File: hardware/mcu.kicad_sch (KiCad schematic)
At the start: 0 parts

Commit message: Kicad şema düzenlemesi yapıldı.
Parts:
- added U4: STM32F103RCTx, Package_QFP:LQFP-64_10x10mm_P0.5mm, symbol MCU_ST_STM32F1:STM32F103RCTx
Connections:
- new net: U4.18 (VSS), U4.31 (VSS), U4.47 (VSS), U4.63 (VSS)
- new net BTN_ACTIVATE: U4.39 (PC8)
- new net BTN_DEACTIVATE: U4.40 (PC9)
- new net BTN_IO: U4.38 (PC7)
- new net I2C_SCL: U4.58 (PB6)
- new net I2C_SDA: U4.59 (PB7)
- new net MCU_ADC_IN: U4.14 (PA0)
- new net MCU_ERROR_LED: U4.36 (PB15)
- new net MCU_RELAY: U4.34 (PB13)
- new net MCU_STATUS_LED: U4.35 (PB14)
- new net RCC_OSC32_IN: U4.3 (PC14)
- new net RCC_OSC32_OUT: U4.4 (PC15)
- new net RCC_OSC_IN: U4.5 (PD0)
- new net RCC_OSC_OUT: U4.6 (PD1)
- new net SPI1_MISO: U4.22 (PA6)
- new net SPI1_MOSI: U4.23 (PA7)
- new net SPI1_SCK: U4.21 (PA5)
- new net SYS_JTCK_SWCLK: U4.49 (PA14)
- new net SYS_JTMS_SWDIO: U4.46 (PA13)
- new net UART_RX: U4.52 (PC11)
- new net UART_TX: U4.51 (PC10)
- new net USAR1_RX: U4.43 (PA10)
- new net USART1_TX: U4.42 (PA9)
- new net USART2_RX: U4.17 (PA3)
- new net USART2_TX: U4.16 (PA2)
- new net USART3_RX: U4.30 (PB11)
- new net USART3_TX: U4.29 (PB10)
- new net USB_DM: U4.44 (PA11)
- new net USB_DP: U4.45 (PA12)
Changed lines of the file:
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@@
 (kicad_sch (version 20230121) (generator eeschema)
   (paper "A4")
+  (hierarchical_label "USB_DP" (shape input) (at 160.02 74.93 0) (fields_autoplaced)
+    (effects (font (size 1.27 1.27)) (justify left))
+  )
+  (hierarchical_label "SPI1_MOSI" (shape output) (at 160.02 62.23 0) (fields_autoplaced)
+    (effects (font (size 1.27 1.27)) (justify left))
+  )
+  (hierarchical_label "RCC_OSC32_IN" (shape input) (at 124.46 100.33 180) (fields_autoplaced)
+    (effects (font (size 1.27 1.27)) (justify right))
+  )
+  (hierarchical_label "BTN_DEACTIVATE" (shape output) (at 124.46 87.63 180) (fields_autoplaced)
+    (effects (font (size 1.27 1.27)) (justify right))
+  )
+  (hierarchical_label "USART3_RX" (shape input) (at 160.02 115.57 0) (fields_autoplaced)
+    (effects (font (size 1.27 1.27)) (justify left))
+  )
+  (hierarchical_label "I2C_SDA" (shape bidirectional) (at 160.02 105.41 0) (fields_autoplaced)
+    (effects (font (size 1.27 1.27)) (justify left))
+  )
+  (hierarchical_label "RCC_OSC_OUT" (shape output) (at 124.46 57.15 180) (fields_autoplaced)
+    (effects (font (size 1.27 1.27)) (justify right))
+  )
+  (hierarchical_label "MCU_ADC_IN" (shape input) (at 160.02 44.45 0) (fields_autoplaced)
+    (effects (font (size 1.27 1.27)) (justify left))
+  )
+  (hierarchical_label "MCU_STATUS_LED" (shape output) (at 160.02 123.19 0) (fields_autoplaced)
+    (effects (font (size 1.27 1.27)) (justify left))
+  )
+  (hierarchical_label "RCC_OSC32_OUT" (shape output) (at 124.46 102.87 180) (fields_autoplaced)
+    (effects (font (size 1.27 1.27)) (justify right))
+  )
+  (hierarchical_label "USAR1_RX" (shape input) (at 160.02 69.85 0) (fields_autoplaced)
+    (effects (font (size 1.27 1.27)) (justify left))
+  )
+  (hierarchical_label "MCU_RELAY" (shape output) (at 160.02 120.65 0) (fields_autoplaced)
+    (effects (font (size 1.27 1.27)) (justify left))
+  )
+  (hierarchical_label "USART2_TX" (shape output) (at 160.02 49.53 0) (fields_autoplaced)
+    (effects (font (size 1.27 1.27)) (justify left))
+  )
+  (hierarchical_label "BTN_ACTIVATE" (shape output) (at 124.46 85.09 180) (fields_autoplaced)
+    (effects (font (size 1.27 1.27)) (justify right))
+  )
+  (hierarchical_label "USART2_RX" (shape input) (at 160.02 52.07 0) (fields_autoplaced)
+    (effects (font (size 1.27 1.27)) (justify left))
+  )
+  (hierarchical_label "I2C_SCL" (shape output) (at 160.02 102.87 0) (fields_autoplaced)
+    (effects (font (size 1.27 1.27)) (justify left))
+  )
+  (hierarchical_label "RCC_OSC_IN" (shape input) (at 124.46 54.61 180) (fields_autoplaced)
+    (effects (font (size 1.27 1.27)) (justify right))
+  )
+  (hierarchical_label "USART1_TX" (shape output) (at 160.02 67.31 0) (fields_autoplaced)
+    (effects (font (size 1.27 1.27)) (justify left))
+  )
+  (hierarchical_label "MCU_ERROR_LED" (shape output) (at 160.02 125.73 0) (fields_autoplaced)
+    (effects (font (size 1.27 1.27)) (justify left))
+  )
+  (hierarchical_label "SYS_JTMS_SWDIO" (shape bidirectional) (at 160.02 77.47 0) (fields_autoplaced)
+    (effects (font (size 1.27 1.27)) (justify left))
+  )
+  (hierarchical_label "USB_DM" (shape output) (at 160.02 72.39 0) (fields_autoplaced)
+    (effects (font (size 1.27 1.27)) (justify left))
+  )
+  (hierarchical_label "BTN_IO" (shape output) (at 124.46 82.55 180) (fields_autoplaced)
+    (effects (font (size 1.27 1.27)) (justify right))
+  )
+  (hierarchical_label "USART3_TX" (shape output) (at 160.02 113.03 0) (fields_autoplaced)
+    (effects (font (size 1.27 1.27)) (justify left))
+  )
+  (hierarchical_label "SPI1_SCK" (shape output) (at 160.02 57.15 0) (fields_autoplaced)
+    (effects (font (size 1.27 1.27)) (justify left))
+  )
+  (hierarchical_label "SPI1_MISO" (shape input) (at 160.02 59.69 0) (fields_autoplaced)
+    (effects (font (size 1.27 1.27)) (justify left))
+  )
+  (hierarchical_label "SYS_JTCK_SWCLK" (shape bidirectional) (at 160.02 80.01 0) (fields_autoplaced)
+    (effects (font (size 1.27 1.27)) (justify left))
+  )
+  (hierarchical_label "UART_TX" (shape output) (at 124.46 90.17 180) (fields_autoplaced)
+    (effects (font (size 1.27 1.27)) (justify right))
+  )
+  (hierarchical_label "UART_RX" (shape input) (at 124.46 92.71 180) (fields_autoplaced)
+    (effects (font (size 1.27 1.27)) (justify right))
+  )
+  (symbol (lib_id "MCU_ST_STM32F1:STM32F103RCTx") (at 142.24 87.63 0) (unit 1)
+    (in_bom yes) (on_board yes) (dnp no) (fields_autoplaced)
+    (property "Reference" "U4" (at 146.9741 133.35 0)
+      (effects (font (size 1.27 1.27)) (justify left))
+    )
+    (property "Value" "STM32F103RCTx" (at 146.9741 135.89 0)
+      (effects (font (size 1.27 1.27)) (justify left))
+    )
+    (property "Footprint" "Package_QFP:LQFP-64_10x10mm_P0.5mm" (at 127 130.81 0)
+      (effects (font (size 1.27 1.27)) (justify right) hide)
+    )
+    (property "Datasheet" "https://www.st.com/resource/en/datasheet/stm32f103rc.pdf" (at 142.24 87.63 0)
+      (effects (font (size 1.27 1.27)) hide)
+    )
+    (pin "1")
+    (pin "10")
+    (pin "11")
+    (pin "12")
+    (pin "13")
+    (pin "14")
+    (pin "15")
+    (pin "16")
+    (pin "17")
+    (pin "18")
+    (pin "19")
+    (pin "2")
+    (pin "20")
+    (pin "21")
+    (pin "22")
+    (pin "23")
+    (pin "24")
+    (pin "25")
+    (pin "26")
+    (pin "27")
+    (pin "28")
+    (pin "29")
+    (pin "3")
+    (pin "30")
+    (pin "31")
+    (pin "32")
+    (pin "33")
+    (pin "34")
+    (pin "35")
+    (pin "36")
+    (pin "37")
+    (pin "38")
+    (pin "39")
+    (pin "4")
+    (pin "40")
+    (pin "41")
+    (pin "42")
+    (pin "43")
+    (pin "44")
+    (pin "45")
+    (pin "46")
+    (pin "47")
+    (pin "48")
+    (pin "49")
+    (pin "5")
+    (pin "50")
+    (pin "51")
+    (pin "52")
+    (pin "53")
+    (pin "54")
+    (pin "55")
+    (pin "56")
+    (pin "57")
+    (pin "58")
+    (pin "59")
+    (pin "6")
+    (pin "60")
+    (pin "61")
+    (pin "62")
+    (pin "63")
+    (pin "64")
+    (pin "7")
+    (pin "8")
+    (pin "9")
+    (instances
+      (project "drip-irrigation-sys-cc"
+        (path "/41708c1e-19b2-4374-83f2-108076d82b45/c9797de2-f042-4c0a-b92d-0b1dd104a99b"
+          (reference "U4") (unit 1)
+        )
+      )
+    )
+  )
 )

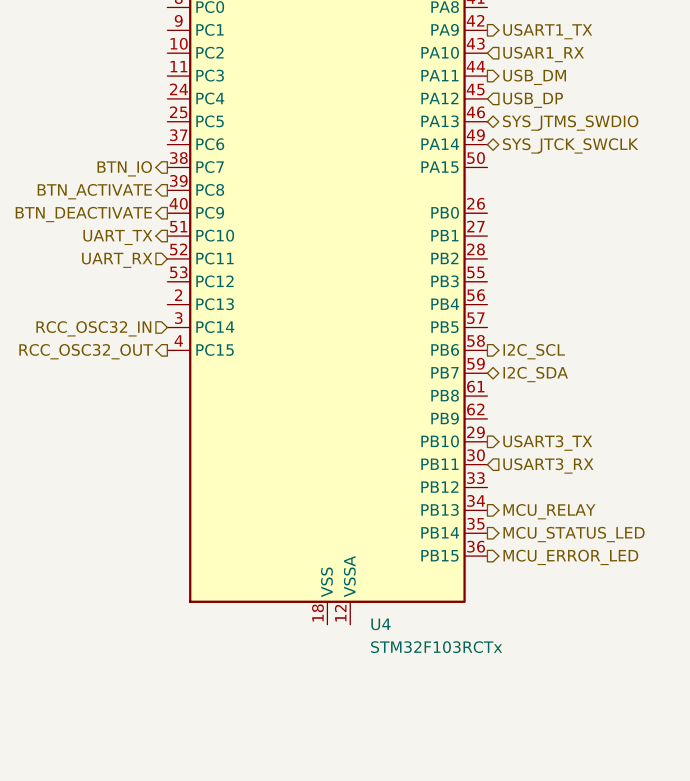
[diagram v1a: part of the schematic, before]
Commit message: Kicad Power Modülü Tamamlandı.
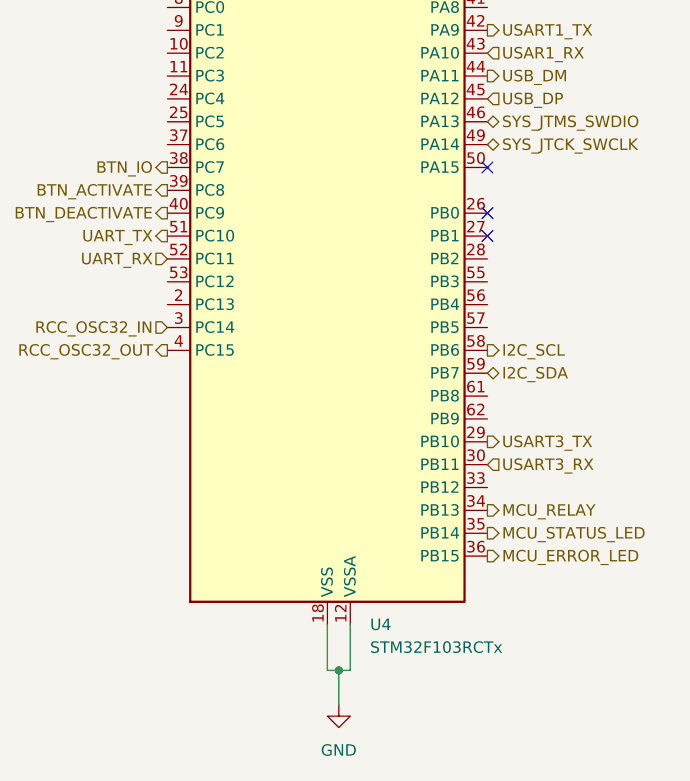
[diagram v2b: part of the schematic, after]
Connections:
- net GND: now reaches U4.12 (VSSA)
- net GND: now also U4.18 (VSS), U4.31 (VSS), U4.47 (VSS), U4.63 (VSS)
- no-connect marks 0 -> 3
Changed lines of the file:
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@@
 (kicad_sch (version 20230121) (generator eeschema)
   (paper "A4")
+  (junction (at 143.51 138.43) (diameter 0) (color 0 0 0 0)
+  )
+  (no_connect (at 160.02 87.63))
+  (no_connect (at 160.02 82.55))
+  (no_connect (at 160.02 90.17))
+  (wire (pts (xy 143.51 138.43) (xy 144.78 138.43))
+    (stroke (width 0) (type default))
+  )
+  (wire (pts (xy 144.78 133.35) (xy 144.78 138.43))
+    (stroke (width 0) (type default))
+  )
+  (wire (pts (xy 142.24 133.35) (xy 142.24 138.43))
+    (stroke (width 0) (type default))
+  )
+  (wire (pts (xy 143.51 138.43) (xy 143.51 142.24))
+    (stroke (width 0) (type default))
+  )
+  (wire (pts (xy 142.24 138.43) (xy 143.51 138.43))
+    (stroke (width 0) (type default))
+  )
   (hierarchical_label "USB_DP" (shape input) (at 160.02 74.93 0) (fields_autoplaced)
     (effects (font (size 1.27 1.27)) (justify left))
@@
         )
       )
+    )
+  )
+  (symbol (lib_id "power:GND") (at 143.51 142.24 0) (unit 1)
+    (in_bom yes) (on_board yes) (dnp no) (fields_autoplaced)
+    (property "Reference" "#PWR06" (at 143.51 148.59 0)
+      (effects (font (size 1.27 1.27)) hide)
+    )
+    (property "Value" "GND" (at 143.51 147.32 0)
+      (effects (font (size 1.27 1.27)))
+    )
+    (property "Footprint" "" (at 143.51 142.24 0)
+      (effects (font (size 1.27 1.27)) hide)
+    )
+    (property "Datasheet" "" (at 143.51 142.24 0)
+      (effects (font (size 1.27 1.27)) hide)
+    )
+    (pin "1")
+    (instances
+      (project "drip-irrigation-sys-cc"
+        (path "/41708c1e-19b2-4374-83f2-108076d82b45/c9797de2-f042-4c0a-b92d-0b1dd104a99b"
+          (reference "#PWR06") (unit 1)
+        )
+      )

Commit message: Kicad şema düzenlemesi yapıldı.
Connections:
- no-connect marks 3 -> 4
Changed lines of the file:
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@@
   )
   (no_connect (at 160.02 87.63))
+  (no_connect (at 160.02 92.71))
   (no_connect (at 160.02 82.55))
   (no_connect (at 160.02 90.17))

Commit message: Kicad düzenleme.
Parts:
- added C15, C16, C17, C18: 10pf, symbol Device:C_Small
- added R12: 10K, symbol Device:R
- added R13: 10mOhm, symbol Device:R
- added Y1: 8MHZ, symbol Device:Crystal_Small
- added Y2: 32KHZ, symbol Device:Crystal_Small
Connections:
- net GND: now also U4.60 (BOOT0), C15.2, C16.2, C17.2, C18.2
- net +3.3V: now reaches U4.1 (VBAT)
- net +3.3V: now also U4.13 (VDDA), U4.19 (VDD), U4.32 (VDD), U4.48 (VDD), U4.64 (VDD), R12.1
- net at U4.7 (NRST): now also R12.2
- net RCC_OSC32_IN: no longer names the net of U4.3 (PC14)
- net RCC_OSC32_IN: now also C17.1, Y2.1
- net RCC_OSC32_OUT: no longer names the net of U4.4 (PC15)
- net RCC_OSC32_OUT: now also C18.1, Y2.2
- net RCC_OSC_IN: no longer names the net of U4.5 (PD0)
- net RCC_OSC_IN: now also C15.1, R13.1, Y1.1
- net RCC_OSC_OUT: no longer names the net of U4.6 (PD1)
- net RCC_OSC_OUT: now also C16.1, R13.2, Y1.2
- no-connect marks 4 -> 20

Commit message: Kicad şema düzenlemesi yapıldı.
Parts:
- added C13, C20, C21, C22: 100nf, Capacitor_SMD:C_0201_0603Metric, symbol Device:C_Small
- added C23: 10nf, Capacitor_SMD:C_1206_3216Metric, symbol Device:C_Small
- added J5: Conn_01x04_Pin, Connector_PinHeader_2.54mm:PinHeader_1x04_P2.54mm_Vertical, symbol Connector:Conn_01x04_Pin
- C15, C16, C17, C18: footprint (none) -> Capacitor_SMD:C_0201_0603Metric; Digikey (none) -> 490-8607-2-ND
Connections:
- net +3.3V: now also C13.2, C20.2, C21.2, C22.2, C23.2
- net GND: now also C13.1, C20.1, C21.1, C22.1, C23.1, J5.4 (Pin_4)
- net SYS_JTCK_SWCLK: no longer names the net of U4.49 (PA14)
- net SYS_JTCK_SWCLK: now also J5.3 (Pin_3)
- net SYS_JTMS_SWDIO: no longer names the net of U4.46 (PA13)
- net SYS_JTMS_SWDIO: now also J5.2 (Pin_2)
- new net +5V: J5.1 (Pin_1)
- no-connect marks 20 -> 22
